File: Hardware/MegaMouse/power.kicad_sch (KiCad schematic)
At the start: 9 parts, among them U501 NCV1117ST50T3G

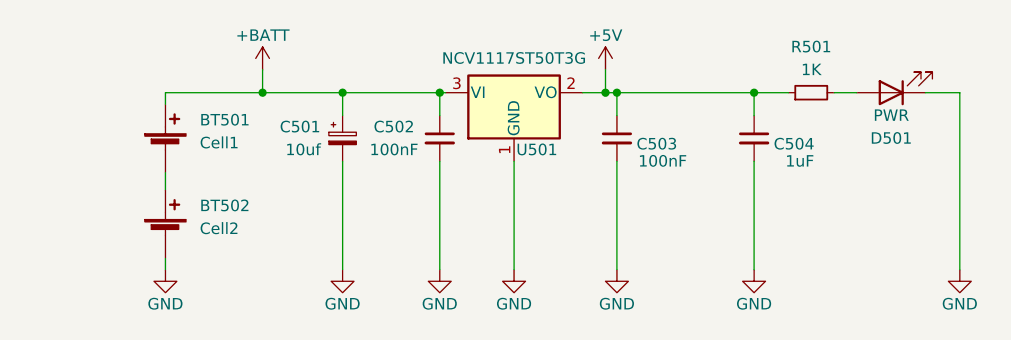
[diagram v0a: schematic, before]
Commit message: Throw on second layer and target a v1.0
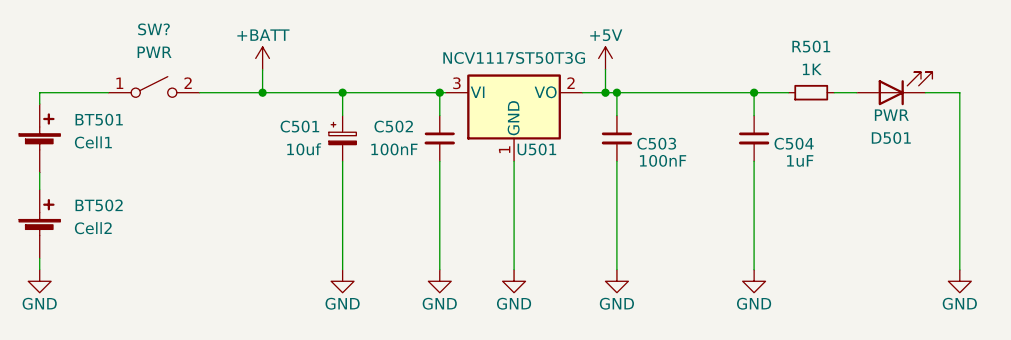
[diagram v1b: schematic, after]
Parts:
- added SW?: PWR, symbol Switch:SW_SPST
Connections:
- net +BATT: now also SW?.2 (B); no longer BT501.1 (+)
- new net: BT501.1 (+), SW?.1 (A)
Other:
- moved on the sheet: BT501, BT502
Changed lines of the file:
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@@
   (junction (at 154.94 88.265) (diameter 0) (color 0 0 0 0)
   )
-  (wire (pts (xy 106.045 88.265) (xy 116.84 88.265))
-    (stroke (width 0) (type default) (color 0 0 0 0))
-  )
-  (wire (pts (xy 106.045 107.95) (xy 106.045 106.68))
+  (wire (pts (xy 92.075 88.265) (xy 99.695 88.265))
+    (stroke (width 0) (type default) (color 0 0 0 0))
+  )
+  (wire (pts (xy 92.075 107.95) (xy 92.075 106.68))
     (stroke (width 0) (type default) (color 0 0 0 0))
   )
@@
     (stroke (width 0) (type default) (color 0 0 0 0))
   )
-  (wire (pts (xy 106.045 88.265) (xy 106.045 89.535))
+  (wire (pts (xy 92.075 88.265) (xy 92.075 89.535))
+    (stroke (width 0) (type default) (color 0 0 0 0))
+  )
+  (wire (pts (xy 109.855 88.265) (xy 116.84 88.265))
     (stroke (width 0) (type default) (color 0 0 0 0))
   )
@@
     (stroke (width 0) (type default) (color 0 0 0 0))
   )
-  (wire (pts (xy 106.045 97.155) (xy 106.045 99.06))
+  (wire (pts (xy 92.075 97.155) (xy 92.075 99.06))
     (stroke (width 0) (type default) (color 0 0 0 0))
   )
@@
     (pin "2")
   )
-  (symbol (lib_name "GND_2") (lib_id "power:GND") (at 106.045 107.95 0) (unit 1)
-    (in_bom yes) (on_board yes)
-    (property "Reference" "#PWR0501" (id 0) (at 106.045 114.3 0)
-      (effects (font (size 1.27 1.27)) hide)
-    )
-    (property "Value" "GND" (id 1) (at 106.045 111.76 0))
-    (property "Footprint" "" (id 2) (at 106.045 107.95 0)
-      (effects (font (size 1.27 1.27)) hide)
-    )
-    (property "Datasheet" "" (id 3) (at 106.045 107.95 0)
+  (symbol (lib_name "GND_2") (lib_id "power:GND") (at 92.075 107.95 0) (unit 1)
+    (in_bom yes) (on_board yes)
+    (property "Reference" "#PWR0501" (id 0) (at 92.075 114.3 0)
+      (effects (font (size 1.27 1.27)) hide)
+    )
+    (property "Value" "GND" (id 1) (at 92.075 111.76 0))
+    (property "Footprint" "" (id 2) (at 92.075 107.95 0)
+      (effects (font (size 1.27 1.27)) hide)
+    )
+    (property "Datasheet" "" (id 3) (at 92.075 107.95 0)
       (effects (font (size 1.27 1.27)) hide)
     )
@@
     (pin "3")
   )
-  (symbol (lib_id "Device:Battery_Cell") (at 106.045 104.14 0) (unit 1)
+  (symbol (lib_id "Device:Battery_Cell") (at 92.075 104.14 0) (unit 1)
     (in_bom yes) (on_board yes) (fields_autoplaced)
-    (property "Reference" "BT502" (id 0) (at 109.855 100.8379 0)
+    (property "Reference" "BT502" (id 0) (at 95.885 100.8379 0)
       (effects (font (size 1.27 1.27)) (justify left))
     )
-    (property "Value" "Cell2" (id 1) (at 109.855 103.3779 0)
+    (property "Value" "Cell2" (id 1) (at 95.885 103.3779 0)
       (effects (font (size 1.27 1.27)) (justify left))
     )
-    (property "Footprint" "Battery:BatteryHolder_MPD_BH-18650-PC2" (id 2) (at 106.045 102.616 90)
-      (effects (font (size 1.27 1.27)) hide)
-    )
-    (property "Datasheet" "~" (id 3) (at 106.045 102.616 90)
+    (property "Footprint" "Battery:BatteryHolder_MPD_BH-18650-PC2" (id 2) (at 92.075 102.616 90)
+      (effects (font (size 1.27 1.27)) hide)
+    )
+    (property "Datasheet" "~" (id 3) (at 92.075 102.616 90)
       (effects (font (size 1.27 1.27)) hide)
     )
@@
     (pin "1")
   )
+  (symbol (lib_id "Switch:SW_SPST") (at 104.775 88.265 0) (unit 1)
+    (in_bom yes) (on_board yes) (fields_autoplaced)
+    (property "Reference" "SW?" (id 0) (at 104.775 81.28 0))
+    (property "Value" "PWR" (id 1) (at 104.775 83.82 0))
+    (property "Footprint" "" (id 2) (at 104.775 88.265 0)
+      (effects (font (size 1.27 1.27)) hide)
+    )
+    (property "Datasheet" "~" (id 3) (at 104.775 88.265 0)
+      (effects (font (size 1.27 1.27)) hide)
+    )
+    (pin "1")
+    (pin "2")
+  )
   (symbol (lib_name "GND_6") (lib_id "power:GND") (at 171.45 107.95 0) (unit 1)
     (in_bom yes) (on_board yes)
@@
     (pin "1")
   )
-  (symbol (lib_id "Device:Battery_Cell") (at 106.045 94.615 0) (unit 1)
+  (symbol (lib_id "Device:Battery_Cell") (at 92.075 94.615 0) (unit 1)
     (in_bom yes) (on_board yes) (fields_autoplaced)
-    (property "Reference" "BT501" (id 0) (at 109.855 91.3129 0)
+    (property "Reference" "BT501" (id 0) (at 95.885 91.3129 0)
       (effects (font (size 1.27 1.27)) (justify left))
     )
-    (property "Value" "Cell1" (id 1) (at 109.855 93.8529 0)
+    (property "Value" "Cell1" (id 1) (at 95.885 93.8529 0)
       (effects (font (size 1.27 1.27)) (justify left))
     )
-    (property "Footprint" "Battery:BatteryHolder_MPD_BH-18650-PC2" (id 2) (at 106.045 93.091 90)
-      (effects (font (size 1.27 1.27)) hide)
-    )
-    (property "Datasheet" "~" (id 3) (at 106.045 93.091 90)
-      (effects (font (size 1.27 1.27)) hide)
-    )
+    (property "Footprint" "Battery:BatteryHolder_MPD_BH-18650-PC2" (id 2) (at 92.075 93.091 90)
+      (effects (font (size 1.27 1.27)) hide)
+    )
+    (property "Datasheet" "~" (id 3) (at 92.075 93.091 90)
+      (effects (font (size 1.27 1.27)) hide)
+    )

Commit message: Even more stuff! also bump libs
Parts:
- SW501: renamed from SW?; footprint (none) -> KenwoodFox:EG1218
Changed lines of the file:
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@@
   (symbol (lib_id "Switch:SW_SPST") (at 104.775 88.265 0) (unit 1)
     (in_bom yes) (on_board yes) (fields_autoplaced)
-    (property "Reference" "SW?" (id 0) (at 104.775 81.28 0))
+    (property "Reference" "SW501" (id 0) (at 104.775 81.28 0))
     (property "Value" "PWR" (id 1) (at 104.775 83.82 0))
-    (property "Footprint" "" (id 2) (at 104.775 88.265 0)
+    (property "Footprint" "KenwoodFox:EG1218" (id 2) (at 104.775 88.265 0)
       (effects (font (size 1.27 1.27)) hide)
     )

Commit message: Bump config
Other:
- company: SNHU -> Kitsune Scientific
- title: Inverted Pendulum Controller -> MegaMouse
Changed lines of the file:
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@@
   (paper "A4")
   (title_block
-    (title "Inverted Pendulum Controller")
+    (title "MegaMouse")
     (date "${ISSUE}")
     (rev "${REVISION}")
-    (company "SNHU")
+    (company "Kitsune Scientific")
     (comment 4 "Release: ${FULL_REVISION}")
   )

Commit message: Awesomeness
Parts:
- removed C502: 100nF, Capacitor_SMD:C_0805_2012Metric, symbol Device:C_Small
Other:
- moved on the sheet: BT501, BT502, C501, SW501

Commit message: Add decoupling caps and 3d models
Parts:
- renumbered C503 to C502, C504 to C503
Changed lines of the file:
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@@
   (symbol (lib_name "GND_1") (lib_id "power:GND") (at 144.78 107.95 0) (unit 1)
     (in_bom yes) (on_board yes)
-    (property "Reference" "#PWR0505" (id 0) (at 144.78 114.3 0)
+    (property "Reference" "#PWR0504" (id 0) (at 144.78 114.3 0)
       (effects (font (size 1.27 1.27)) hide)
     )
@@
   (symbol (lib_id "Device:C_Small") (at 156.21 93.345 0) (unit 1)
     (in_bom yes) (on_board yes)
-    (property "Reference" "C503" (id 0) (at 160.655 93.98 0))
+    (property "Reference" "C502" (id 0) (at 160.655 93.98 0))
     (property "Value" "100nF" (id 1) (at 161.29 95.885 0))
     (property "Footprint" "Capacitor_SMD:C_0805_2012Metric" (id 2) (at 156.21 93.345 0)
@@
   (symbol (lib_name "GND_5") (lib_id "power:GND") (at 156.21 107.95 0) (unit 1)
     (in_bom yes) (on_board yes)
-    (property "Reference" "#PWR0507" (id 0) (at 156.21 114.3 0)
+    (property "Reference" "#PWR0506" (id 0) (at 156.21 114.3 0)
       (effects (font (size 1.27 1.27)) hide)
     )
@@
   (symbol (lib_id "Device:C_Small") (at 171.45 93.345 0) (unit 1)
     (in_bom yes) (on_board yes)
-    (property "Reference" "C504" (id 0) (at 175.895 93.98 0))
+    (property "Reference" "C503" (id 0) (at 175.895 93.98 0))
     (property "Value" "1uF" (id 1) (at 176.53 95.885 0))
     (property "Footprint" "Capacitor_SMD:C_0805_2012Metric" (id 2) (at 171.45 93.345 0)
@@
   (symbol (lib_id "power:GND") (at 194.31 107.95 0) (unit 1)
     (in_bom yes) (on_board yes)
-    (property "Reference" "#PWR0509" (id 0) (at 194.31 114.3 0)
+    (property "Reference" "#PWR0508" (id 0) (at 194.31 114.3 0)
       (effects (font (size 1.27 1.27)) hide)
     )
@@
   (symbol (lib_id "power:+5V") (at 154.94 85.725 0) (unit 1)
     (in_bom yes) (on_board yes)
-    (property "Reference" "#PWR0506" (id 0) (at 154.94 89.535 0)
+    (property "Reference" "#PWR0505" (id 0) (at 154.94 89.535 0)
       (effects (font (size 1.27 1.27)) hide)
     )
@@
   (symbol (lib_name "GND_6") (lib_id "power:GND") (at 171.45 107.95 0) (unit 1)
     (in_bom yes) (on_board yes)
-    (property "Reference" "#PWR0508" (id 0) (at 171.45 114.3 0)
+    (property "Reference" "#PWR0507" (id 0) (at 171.45 114.3 0)
       (effects (font (size 1.27 1.27)) hide)
     )

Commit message: Verification 1 (#3)
And thats all we have time for folks.
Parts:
- BT501, BT502: LCSC# (none) -> C5290176
- SW501: LCSC# (none) -> C273394
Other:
- moved on the sheet: BT501, BT502, C501, C502, C503, D501, R501, SW501, U501
